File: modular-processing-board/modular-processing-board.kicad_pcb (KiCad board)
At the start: 6 copper layers, 90 x 90 mm, 166 parts, among them J1001 BWU.FL-IPEX1, J202 Conn_02x06_Odd_Even, J401 TF01A, J501 Plug_Hirose_DF40_2x40_DF40C-8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, J502 Conn_02x06_Odd_Even, J601 Conn_Coaxial_Small, J602 BWU.FL-IPEX1, J604 Conn_Coaxial_Small, J701 Conn_02x02_Odd_Even, J801 TYPE-C-31-M-12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

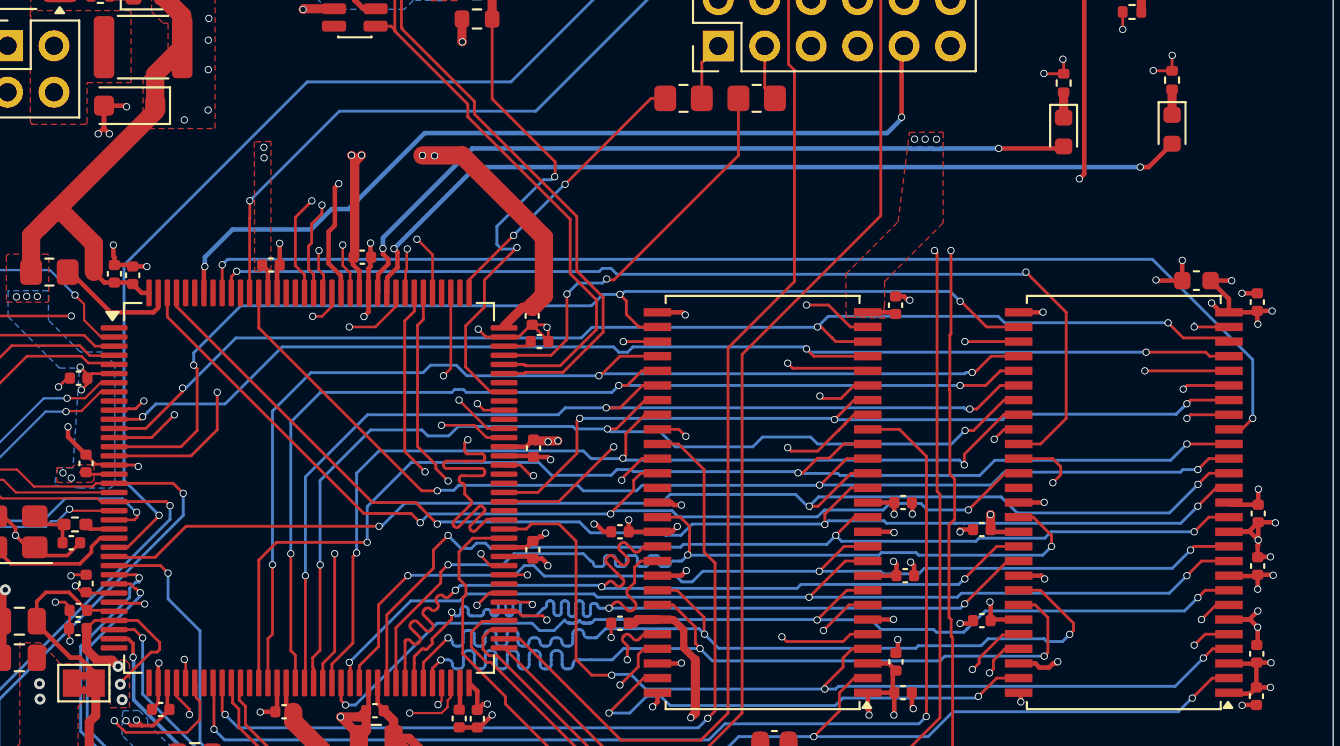
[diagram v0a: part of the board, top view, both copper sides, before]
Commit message: changeed layer 3 traces to 50 ohm-impedance tracks
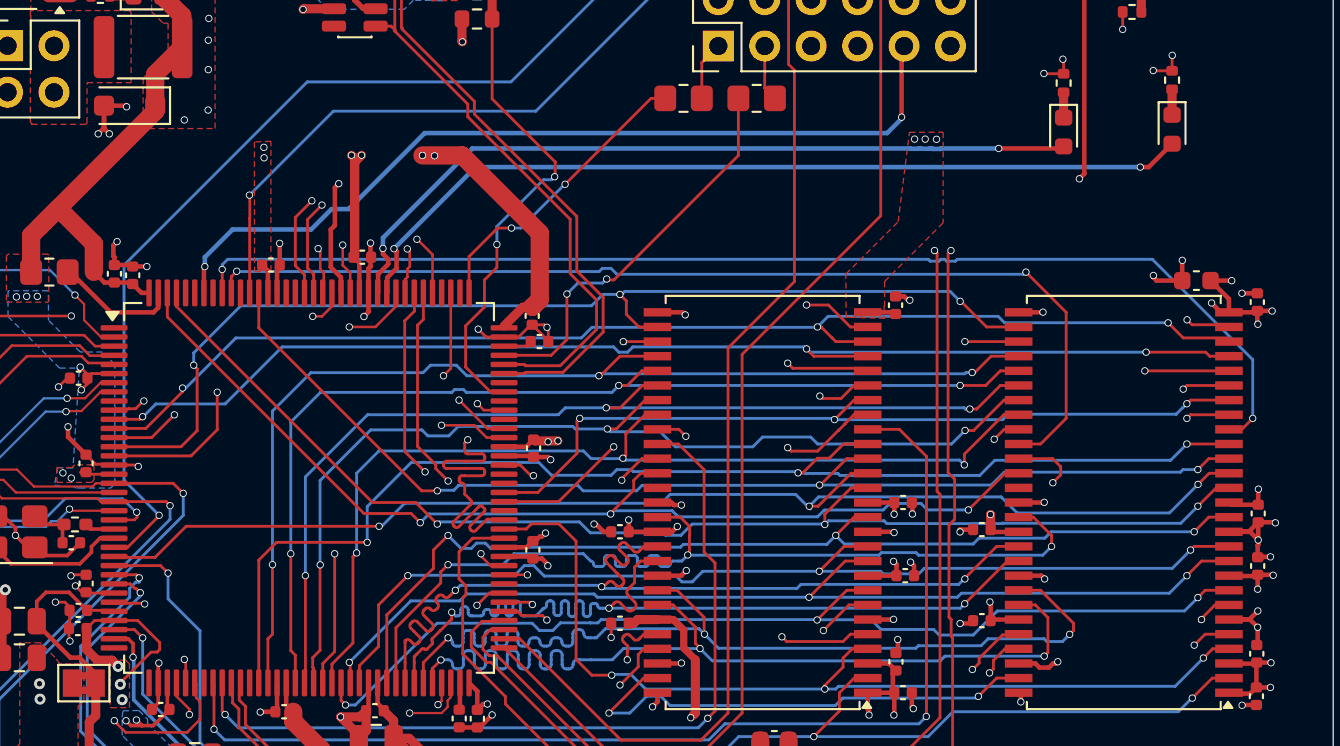
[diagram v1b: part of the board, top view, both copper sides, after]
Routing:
- net /mcu/USB_SENSE: track 28.5 -> 27.0 mm
- net /mcu/SWD_SWCLK: track 15.5 -> 16.3 mm
- net GND: track 243.9 -> 244.5 mm
- added copper zone on In2.Cu, net GND

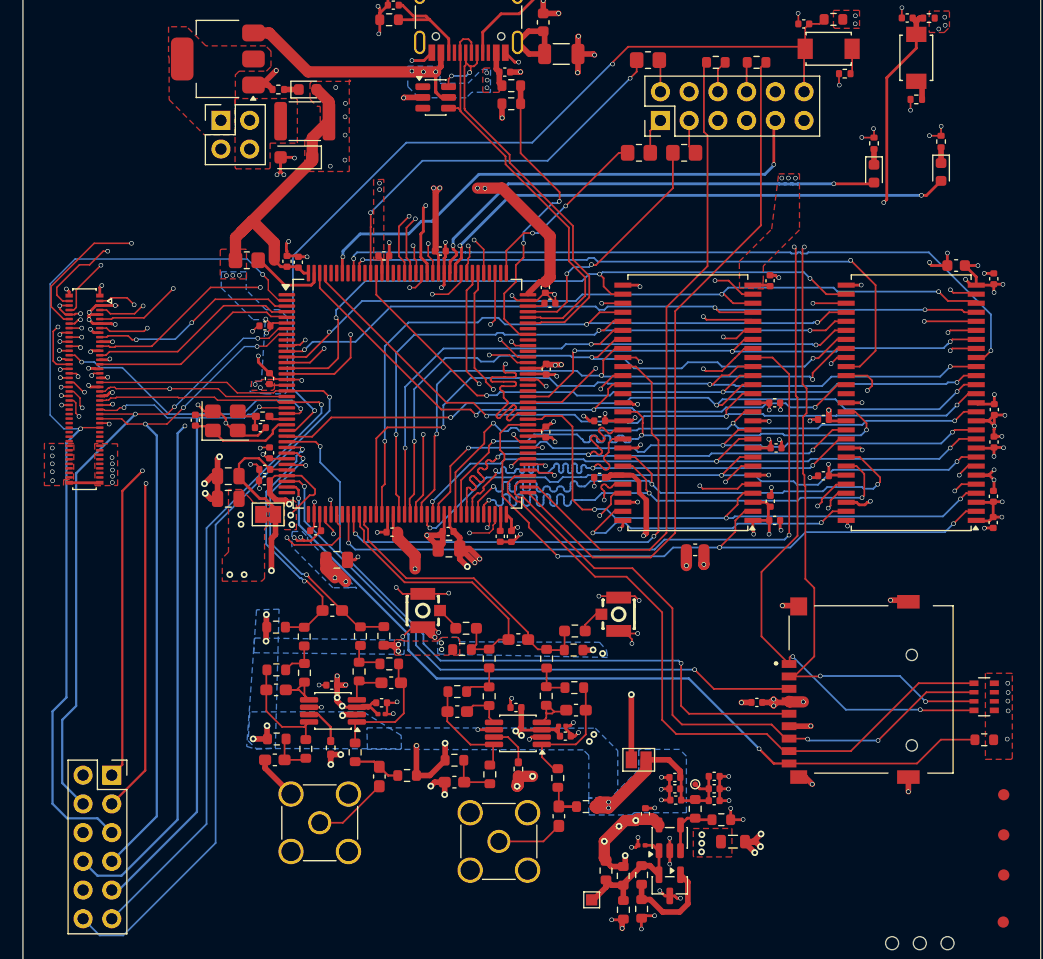
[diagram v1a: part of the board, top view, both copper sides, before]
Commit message: added return  vias, solved routing errors (next) check impedance of top-bottom layer signals, schematic check
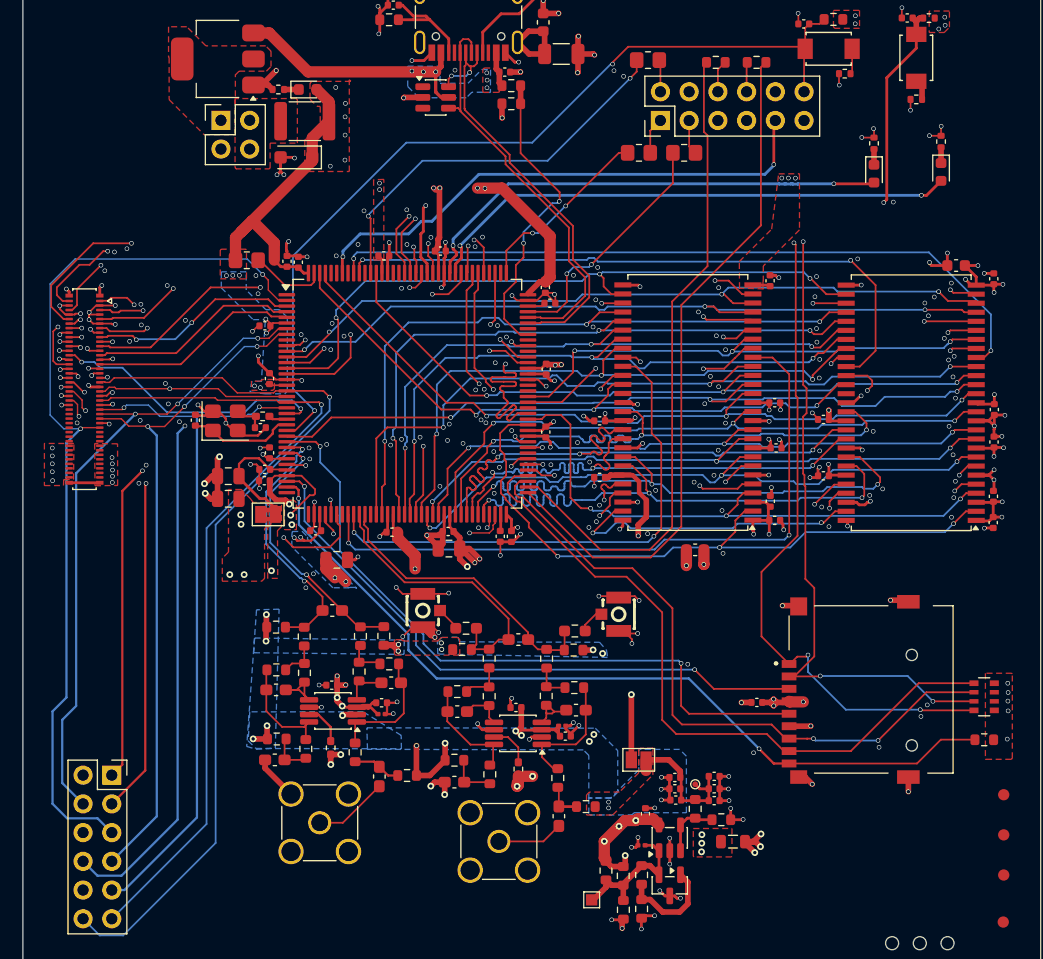
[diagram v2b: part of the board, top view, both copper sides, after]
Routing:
- net /adc-frontend/MCU_VREF: track 60.3 -> 16.9 mm
- net /adc-frontend/VOCM_BUFF: track 38.7 -> 31.5 mm
- net +3V3: track 157.9 -> 152.8 mm
- net GND: track 244.5 -> 247.9 mm, vias 162 -> 279
- net /mcu/SDRAM.D13: track 51.7 -> 54.0 mm
- net /mcu/SDRAM.D15: track 55.7 -> 54.0 mm
- net /mcu/SDMMC.D2: track 98.4 -> 99.9 mm
- net /mcu/SDRAM.A1: track 66.6 -> 67.5 mm
- net /mcu/SDRAM.D9: track 50.3 -> 51.1 mm
- net /connectors/PSSI.D1: track 42.8 -> 42.0 mm
- net /mcu/SDRAM.A9: track 56.2 -> 55.6 mm
- added copper zone on F.Cu, net /adc-frontend/MCU_VREF
- added copper zone on In3.Cu, net /adc-frontend/MCU_VREF

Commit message: completed schematic + layout (next) do footprint checks etc.
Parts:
- added TP201: TestPoint, iw-misc:TestPoint_Pad_D0.5mm, F.Cu at (57.4, 33.4)
- added TP202: TestPoint, iw-misc:TestPoint_Pad_D0.5mm, F.Cu at (57.4, 36.4)
- added TP402: TestPoint, iw-misc:TestPoint_Pad_D0.5mm, F.Cu at (52.3, 36.4)
- added TP403: TestPoint, iw-misc:TestPoint_Pad_D0.5mm, F.Cu at (57.0, 41.0)
- added TP404: TestPoint, iw-misc:TestPoint_Pad_D0.5mm, F.Cu at (-9.74, -7.12)
- moved FID104 101.2 mm to (72.8, 53.6)
- moved H103 81.5 mm to (133.3, 54.2)
- moved FID103 70.8 mm to (63.9, 131.6)
- moved FID102 69.1 mm to (131.5, 57.0)
- moved H102 61.0 mm to (66.5, 130.7)
- moved FID101 10.6 mm to (127.1, 129.8)
- moved H101 6.78 mm to (122.1, 129.4)
- moved JP202 1.48 mm to (69.1, 99.0)
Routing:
- net +3V3: track 152.8 -> 89.3 mm, vias 70 -> 75
- net GND: track 247.9 -> 229.7 mm, vias 279 -> 282
- net VDDA: track 41.3 -> 30.6 mm
- net /adc-frontend/MCU_VREF: track 16.9 -> 8.05 mm
- net /usb/USB_SH: track 33.9 -> 26.5 mm
- added copper zone on F.Cu, net /usb/USB_SH

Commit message: checking SDMMC SD-card interface (next) finish checking sd-card holder, check connectors, frontend and power
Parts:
- removed C815: 1nF, Capacitor_SMD:C_1206_3216Metric
- removed L801: 120@100MHz, Inductor_SMD:L_0603_1608Metric
- moved TP404 106.7 mm to (75.4, 57.2)
- moved TP202 64.1 mm to (65.2, 100.0)
- moved TP403 42.6 mm to (97.7, 53.5)
- moved TP201 38.3 mm to (68.8, 69.9)
- moved TP402 32.6 mm to (81.5, 50.9)
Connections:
- J801 pad S1: /usb/USB_SH -> GND
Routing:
- net /usb/USB_SH: track 26.5 -> 0.00 mm
- net GND: track 229.7 -> 256.0 mm, vias 282 -> 278
- net /usb/USB_CC1: track 10.7 -> 18.6 mm, vias 0 -> 2
- net /usb/USB_CC2: track 9.65 -> 11.5 mm
- net /power/USB_VBUS: track 26.5 -> 28.0 mm
- net +3V3: track 89.3 -> 90.7 mm
- net VDDA: track 30.6 -> 31.7 mm
- removed copper zone on F.Cu, net /usb/USB_SH

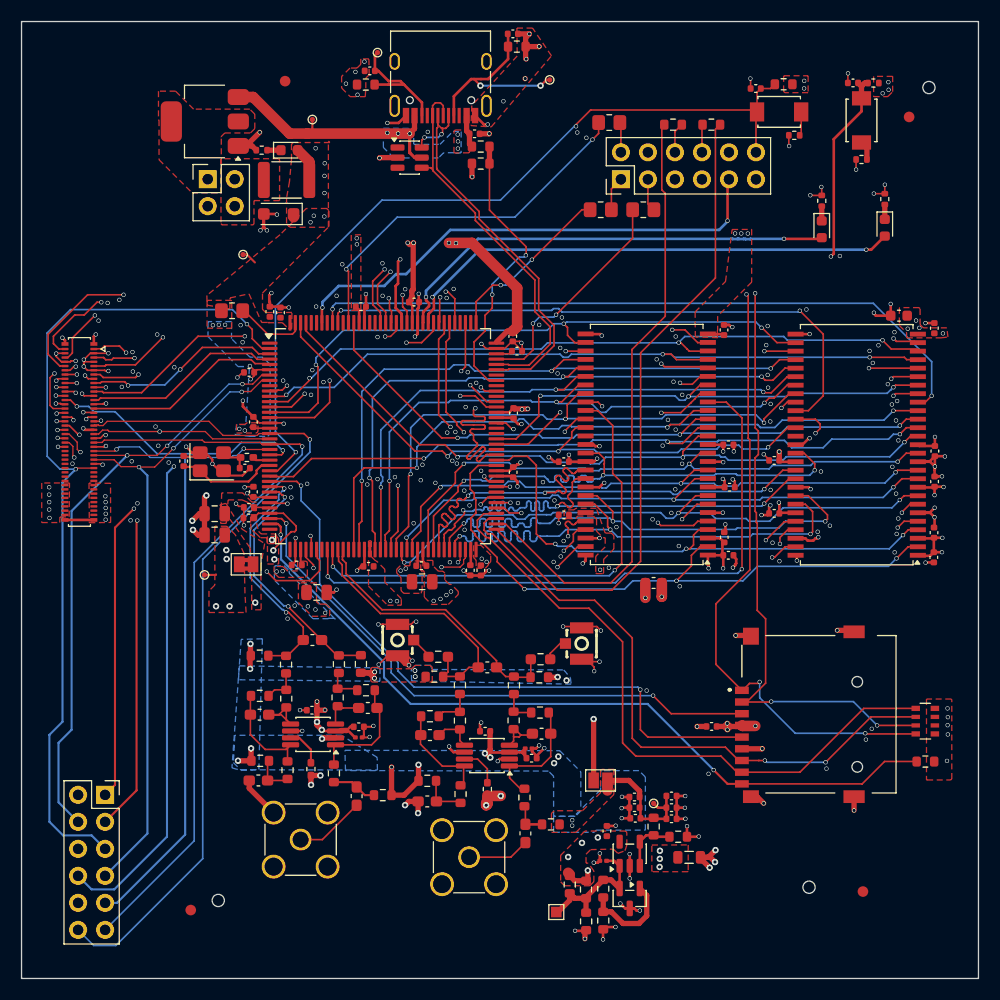
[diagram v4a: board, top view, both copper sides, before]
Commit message: finished schematic checks, added extra capacitors on LDO output (next) add holes to board / board shape, do layout checks
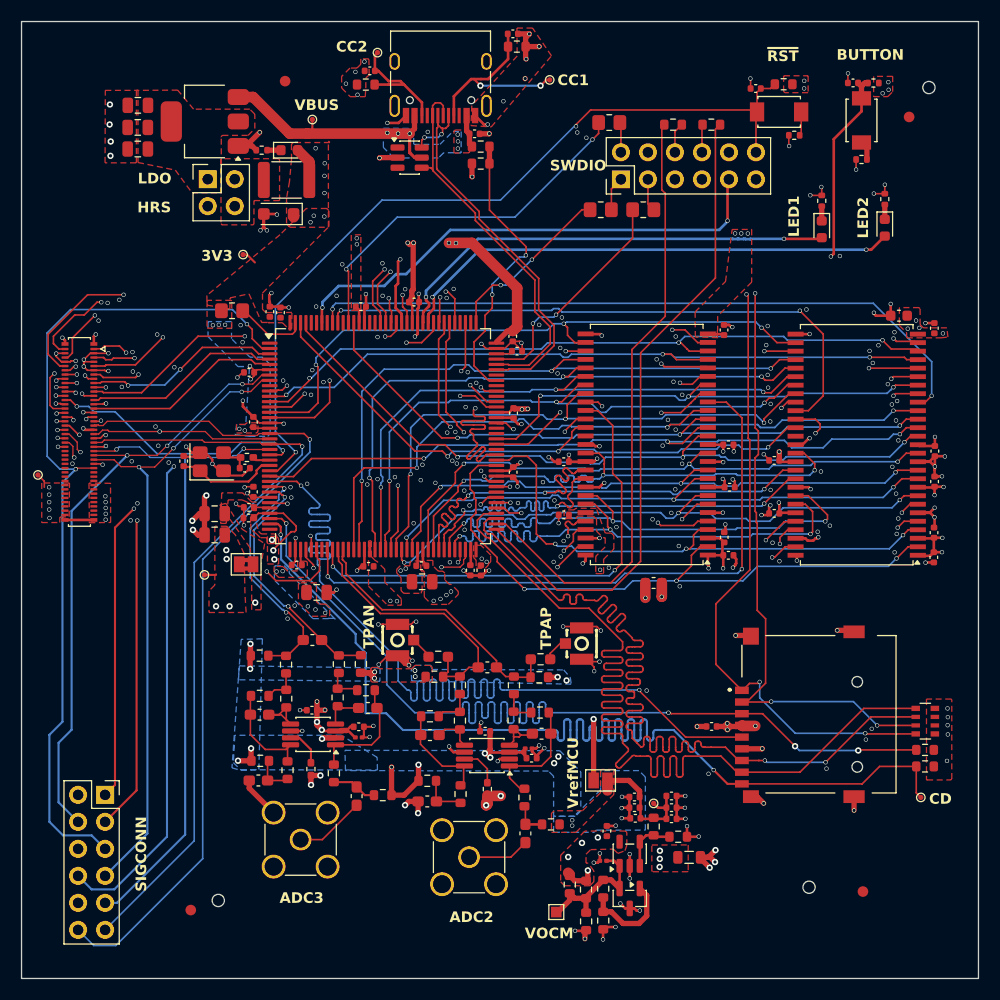
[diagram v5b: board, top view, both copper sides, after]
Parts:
- added C701: 22uF, Capacitor_SMD:C_0805_2012Metric, F.Cu at (58.9, 55.9)
- added C702: 22uF, Capacitor_SMD:C_0805_2012Metric, F.Cu at (58.9, 58.0)
- added C703: 22uF, Capacitor_SMD:C_0805_2012Metric, F.Cu at (58.9, 60.0)
- added R402: 10k, Resistor_SMD:R_0603_1608Metric, F.Cu at (133.0, 116.5)
- added TP401: TestPoint, iw-misc:TestPoint_Pad_D0.5mm, F.Cu at (132.6, 121.0)
- added TP701: TestPoint, iw-misc:TestPoint_Pad_D0.5mm, F.Cu at (49.5, 90.6)
- moved R401 0.46 mm to (133.0, 118.1)
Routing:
- net /mcu/SDMMC.CMD: track 54.5 -> 95.1 mm, vias 2 -> 4
- net /mcu/SDMMC.D1: track 61.8 -> 99.7 mm
- net /mcu/SDMMC.D0: track 58.9 -> 94.4 mm
- net /mcu/SDMMC.CK: track 61.5 -> 95.7 mm
- net /mcu/SDMMC.CD: track 74.5 -> 105.1 mm
- net /connectors/HRS_3V3: track 0.00 -> 1.40 mm
- net GND: vias 278 -> 282
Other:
- board text added: "3V3"
- board text added: "ADC2"
- board text added: "ADC3"
- board text added: "BUTTON"
- board text added: "CC1"
- board text added: "CC2"
- board text added: "CD"
- board text added: "HRS"
- board text added: "LDO"
- board text added: "LED1"
- board text added: "LED2"
- board text added: "SIGCONN"
- board text added: "SWDIO"
- board text added: "TPAN"
- board text added: "TPAP"
- board text added: "VBUS"
- board text added: "VOCM"
- board text added: "VrefMCU"
- board text added: "~{RST}"
